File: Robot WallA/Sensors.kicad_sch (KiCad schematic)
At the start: 20 parts, among them J34 Conn_01x03, J35 SM04B-SRSS-TB, J36 SM04B-SRSS-TB, J37 SM04B-SRSS-TB, J38 SM02B-SRSS-TB_LF__SN_, J39 Conn_01x03, J40 SM03B-SRSS-TB_LF__SN_, J41 SM03B-SRSS-TB_LF__SN_, J42 SM03B-SRSS-TB_LF__SN_, J43 SM03B-SRSS-TB_LF__SN_, J44 SM02B-SRSS-TB_LF__SN_, J45 SM04B-SRSS-TB, J46 SM02B-SRSS-TB_LF__SN_, J47 SM02B-SRSS-TB_LF__SN_

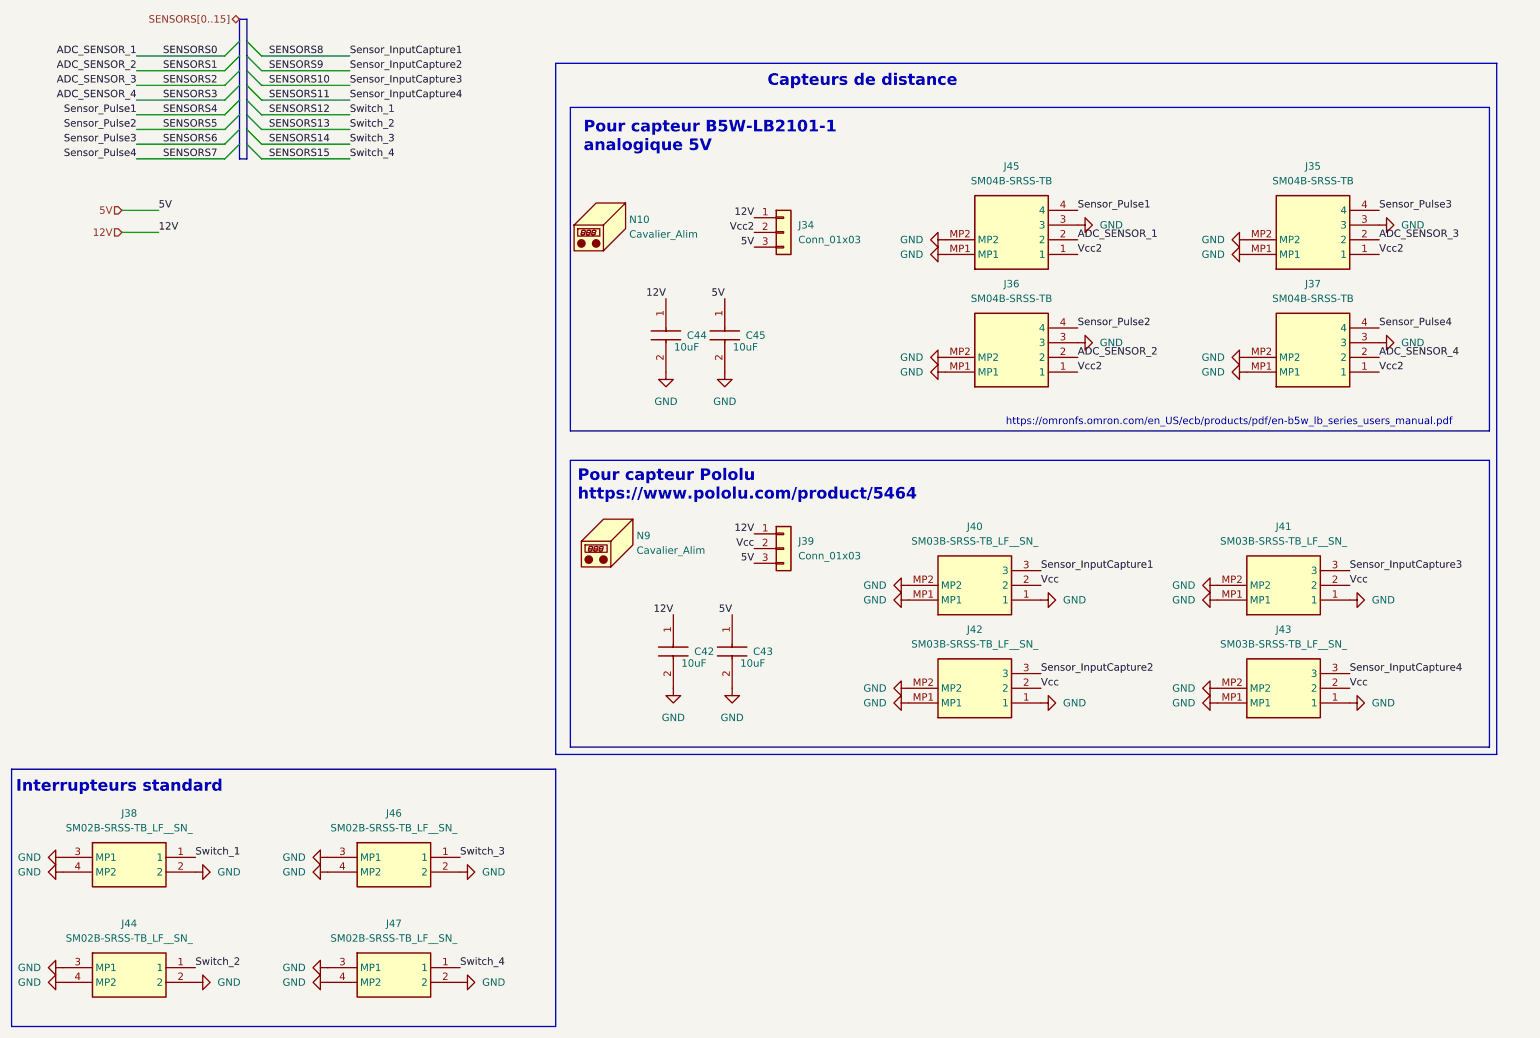
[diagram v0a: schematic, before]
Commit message: Corrected schematic labels encoders according to PCB labels... (inversion...)
Add fab files
cleaned
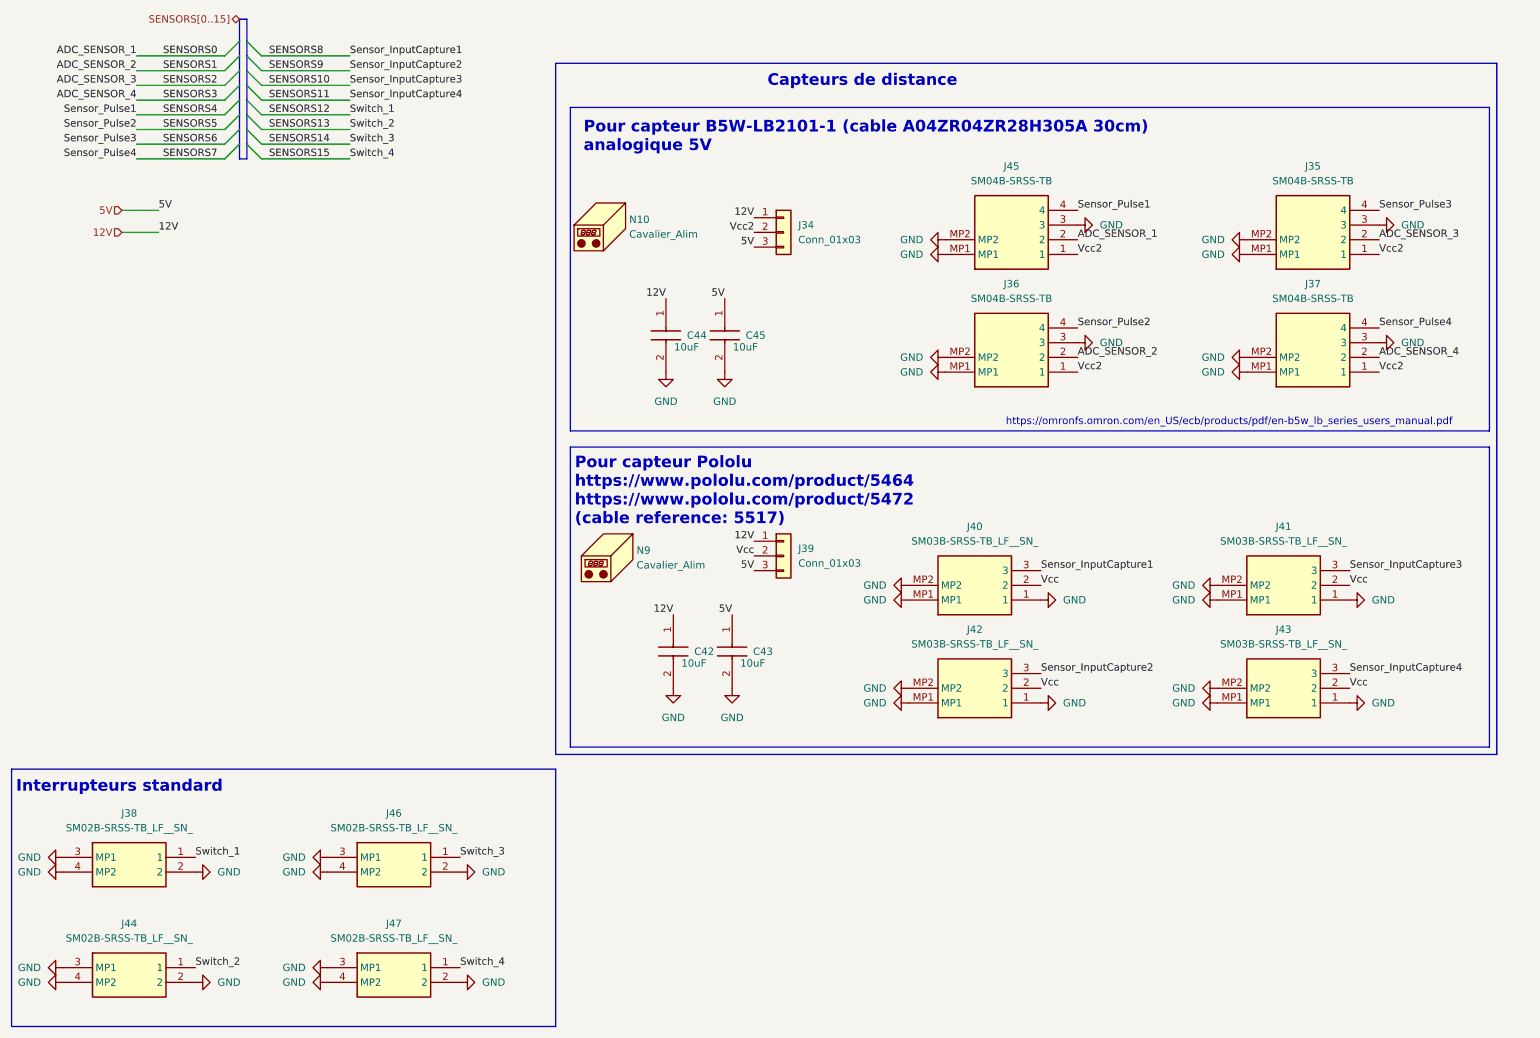
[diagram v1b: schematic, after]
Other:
- note added: "Pour capteur B5W-LB2101-1 (cable A04ZR04ZR28H305A 30cm) analogique 5V"
- note added: "Pour capteur Pololu https://www.pololu.com/product/5464 https://www.pololu.com/product/5472 (cable reference: 5517)"
- note removed: "Pour capteur B5W-LB2101-1 analogique 5V"
- note removed: "Pour capteur Pololu https://www.pololu.com/product/5464"
- moved on the sheet: J39, N9
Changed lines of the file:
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@@
 	)
 	(rectangle
-		(start 118.11 96.52)
+		(start 118.11 94.234)
 		(end 276.86 146.05)
 		(stroke
@@
 		)
 	)
-	(text "Pour capteur Pololu\nhttps://www.pololu.com/product/5464"
+	(text "Pour capteur Pololu\nhttps://www.pololu.com/product/5464\nhttps://www.pololu.com/product/5472\n(cable reference: 5517)"
 		(exclude_from_sim no)
-		(at 119.38 100.838 0)
+		(at 118.872 101.854 0)
 		(effects
 			(font
@@
 		)
 	)
-	(text "Pour capteur B5W-LB2101-1\nanalogique 5V"
+	(text "Pour capteur B5W-LB2101-1 (cable A04ZR04ZR28H305A 30cm)\nanalogique 5V"
 		(exclude_from_sim no)
 		(at 120.396 40.64 0)
@@
 	)
 	(label "12V"
-		(at 149.86 109.22 180)
+		(at 149.86 110.49 180)
 		(effects
 			(font
@@
 	)
 	(label "Vcc"
-		(at 149.86 111.76 180)
+		(at 149.86 113.03 180)
 		(effects
 			(font
@@
 	)
 	(label "5V"
-		(at 149.86 114.3 180)
+		(at 149.86 115.57 180)
 		(effects
 			(font
@@
 	(symbol
 		(lib_id "Mechanical:Housing")
-		(at 125.73 110.49 0)
+		(at 125.73 113.03 0)
 		(unit 1)
 		(exclude_from_sim no)
@@
 		(dnp no)
 		(property "Reference" "N9"
-			(at 129.54 109.5374 0)
+			(at 129.54 112.0774 0)
 			(effects
 				(font
@@
 		)
 		(property "Value" "Cavalier_Alim"
-			(at 129.54 112.0774 0)
+			(at 129.54 114.6174 0)
 			(effects
 				(font
@@
 		)
 		(property "Footprint" ""
-			(at 127 109.22 0)
+			(at 127 111.76 0)
 			(effects
 				(font
@@
 		)
 		(property "Datasheet" "~"
-			(at 127 109.22 0)
+			(at 127 111.76 0)
 			(effects
 				(font
@@
 		)
 		(property "Description" "Housing"
-			(at 125.73 110.49 0)
+			(at 125.73 113.03 0)
 			(effects
 				(font
@@
 		)
 		(property "Manufacturer_Part_Number" "15-29-1024"
-			(at 125.73 110.49 0)
+			(at 125.73 113.03 0)
 			(effects
 				(font
@@
 		)
 		(property "Arrow Part Number" ""
-			(at 125.73 110.49 0)
+			(at 125.73 113.03 0)
 			(effects
 				(font
@@
 		)
 		(property "Arrow Price/Stock" ""
-			(at 125.73 110.49 0)
+			(at 125.73 113.03 0)
 			(effects
 				(font
@@
 		)
 		(property "Mouser Price/Stock" ""
-			(at 125.73 110.49 0)
+			(at 125.73 113.03 0)
 			(effects
 				(font
@@
 	(symbol
 		(lib_id "Connector_Generic:Conn_01x03")
-		(at 154.94 111.76 0)
+		(at 154.94 113.03 0)
 		(unit 1)
 		(exclude_from_sim no)
@@
 		(fields_autoplaced yes)
 		(property "Reference" "J39"
-			(at 157.48 110.4899 0)
+			(at 157.48 111.7599 0)
 			(effects
 				(font
@@
 		)
 		(property "Value" "Conn_01x03"
-			(at 157.48 113.0299 0)
+			(at 157.48 114.2999 0)
 			(effects
 				(font
@@
 		)
 		(property "Footprint" "Connector_PinHeader_2.54mm:PinHeader_1x03_P2.54mm_Vertical"
-			(at 154.94 111.76 0)
+			(at 154.94 113.03 0)
 			(effects
 				(font
@@
 		)
 		(property "Datasheet" "~"
-			(at 154.94 111.76 0)
+			(at 154.94 113.03 0)
 			(effects
 				(font
@@
 		)
 		(property "Description" "Generic connector, single row, 01x03, script generated (kicad-library-utils/schlib/autogen/connector/)"
-			(at 154.94 111.76 0)
+			(at 154.94 113.03 0)
 			(effects
 				(font
@@
 		)
 		(property "Arrow Part Number" ""
-			(at 154.94 111.76 0)
+			(at 154.94 113.03 0)
 			(effects
 				(font
@@
 		)
 		(property "Arrow Price/Stock" ""
-			(at 154.94 111.76 0)
+			(at 154.94 113.03 0)
 			(effects
 				(font
@@
 		)
 		(property "Mouser Price/Stock" ""
-			(at 154.94 111.76 0)
+			(at 154.94 113.03 0)
 			(effects
 				(font
